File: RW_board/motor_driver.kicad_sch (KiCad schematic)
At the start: 22 parts, among them IC1 MCT8316Z0RQRGFRQ1

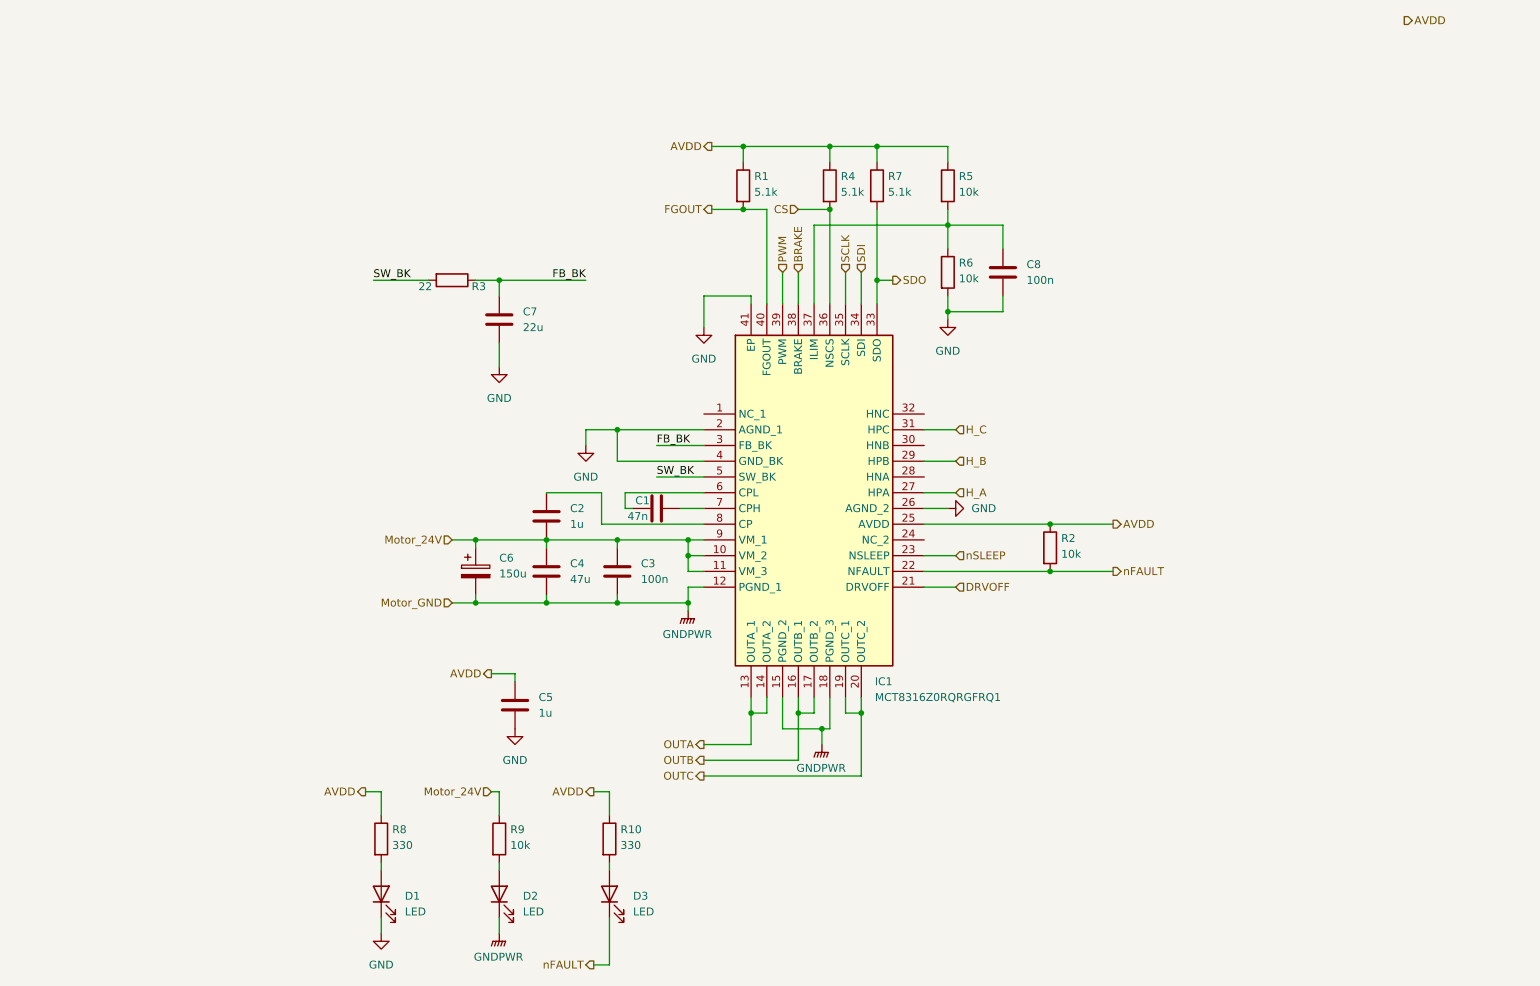
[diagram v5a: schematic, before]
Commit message: Switched motor, added connectors, finished up design
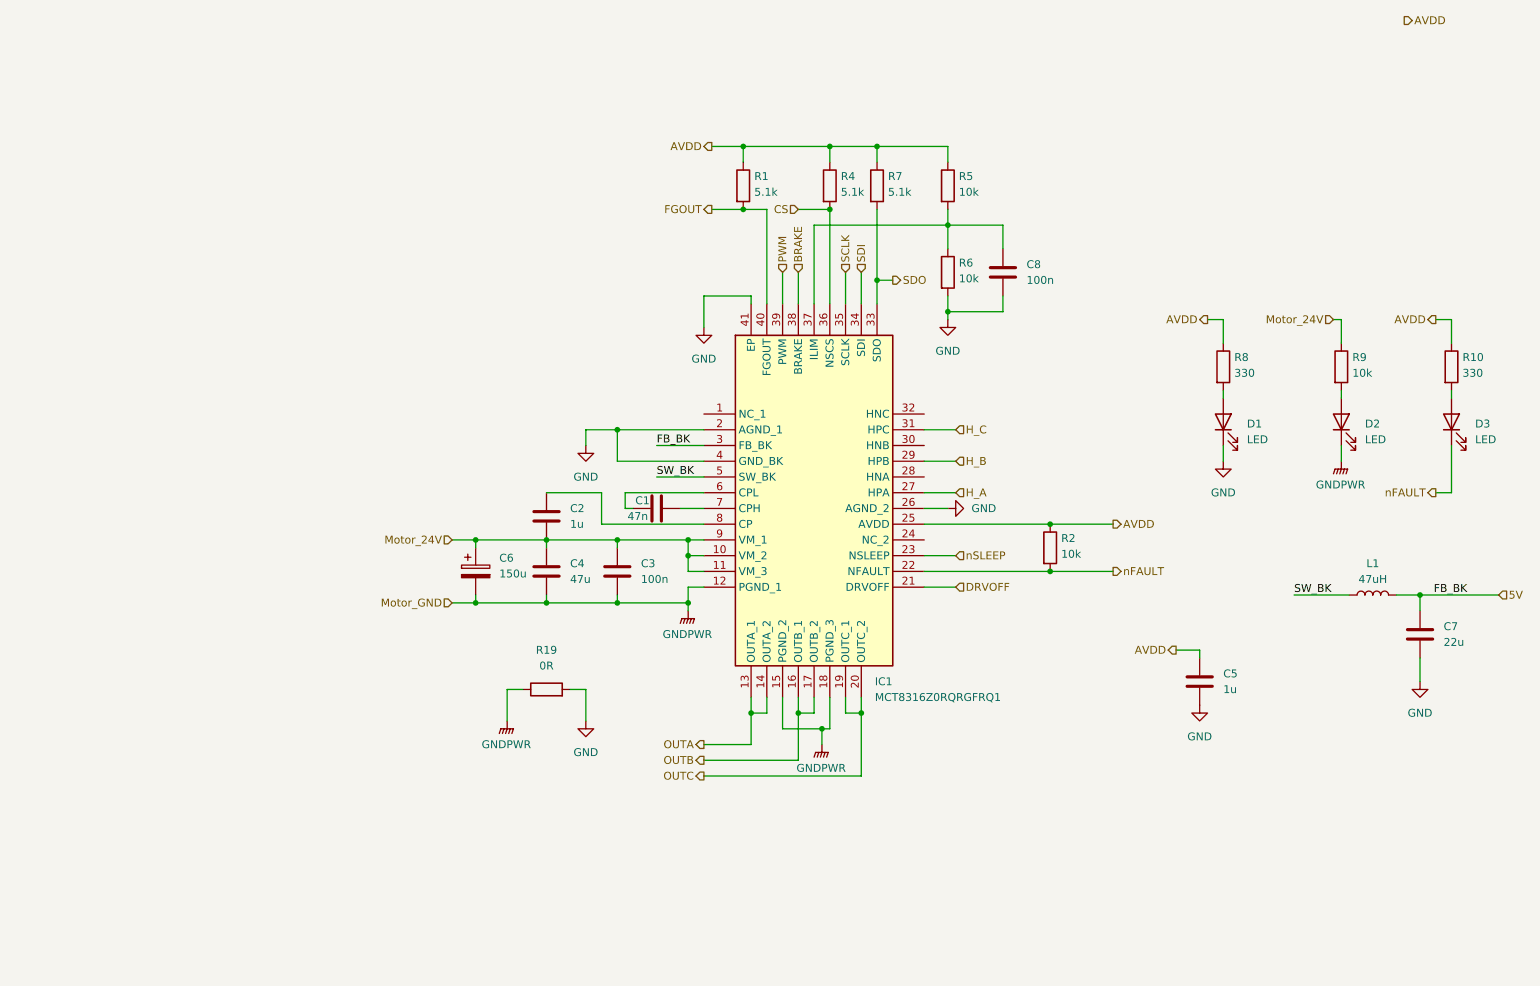
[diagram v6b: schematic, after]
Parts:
- removed R3: 22, Capacitor_SMD:C_0402_1005Metric, symbol Device:R
- added L1: 47uH, Inductor_SMD:L_1210_3225Metric, symbol Device:L
- added R19: 0R, Resistor_SMD:R_0805_2012Metric, symbol Device:R
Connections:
- net GND: now also R19.2
- net GNDPWR: now also R19.1
- net SW_BK: now also L1.1
- net FB_BK renamed 5V
- net 5V: now also L1.2
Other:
- moved on the sheet: C5, C7, D1, D2, D3, R10, R8, R9

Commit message: Fixed reset switch
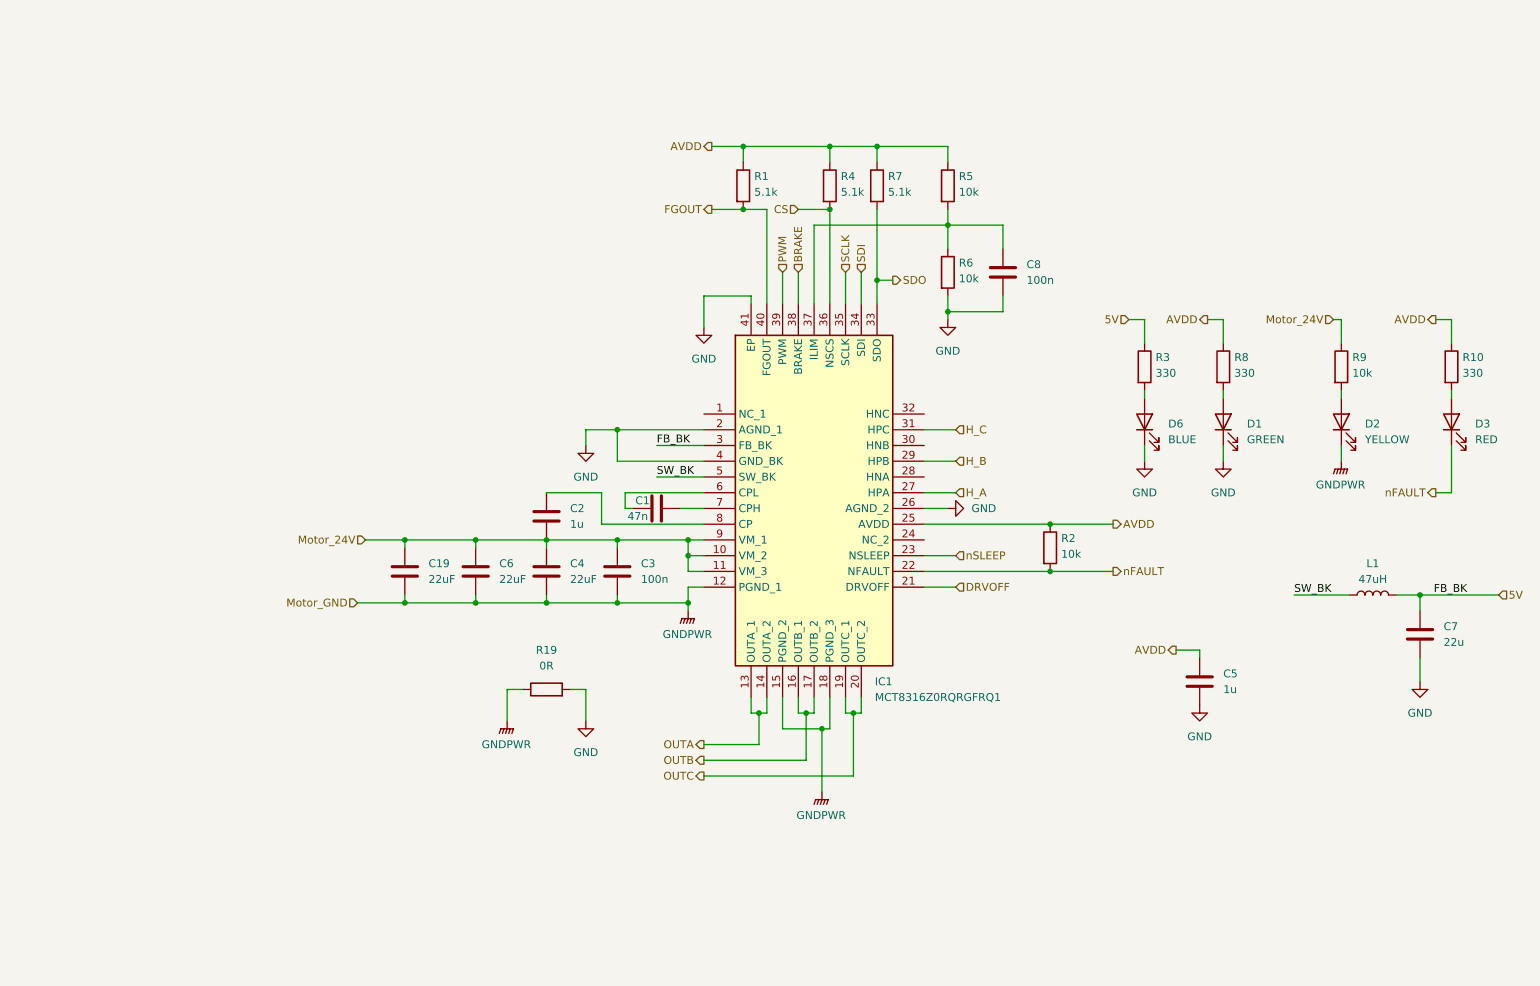
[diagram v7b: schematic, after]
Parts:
- removed C6: 150u, Capacitor_SMD:CP_Elec_6.3x7.7, symbol Device:C_Polarized
- added C19, C6: 22uF, Capacitor_SMD:C_0805_2012Metric, symbol Device:C
- added D6: BLUE, LED_SMD:LED_0603_1608Metric, symbol Device:LED
- added R3: 330, Resistor_SMD:R_0402_1005Metric, symbol Device:R
- C4: value 47u -> 22uF; Voltage rating 30V -> 35V
- D1: value LED -> GREEN; footprint (none) -> LED_SMD:LED_0603_1608Metric
- D2: value LED -> YELLOW; footprint (none) -> LED_SMD:LED_0603_1608Metric
- D3: value LED -> RED; footprint (none) -> LED_SMD:LED_0603_1608Metric
- R1, R10, R2, R4, R5, R6, R7, R8, R9: footprint (none) -> Resistor_SMD:R_0402_1005Metric
- R19: footprint Resistor_SMD:R_0805_2012Metric -> Capacitor_SMD:C_0201_0603Metric
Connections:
- net 5V: now also R3.1
- net GND: now also D6.1 (K)
- net GNDPWR: now also C19.2, C6.2
- net Motor_24V: now also C19.1, C6.1
- new net: D6.2 (A), R3.2

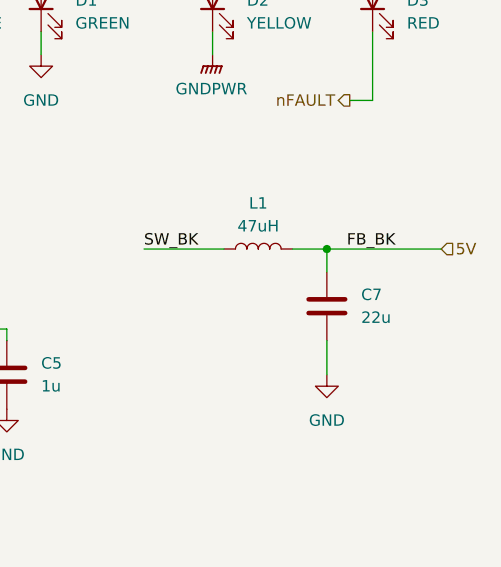
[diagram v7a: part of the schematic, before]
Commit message: Fixed text
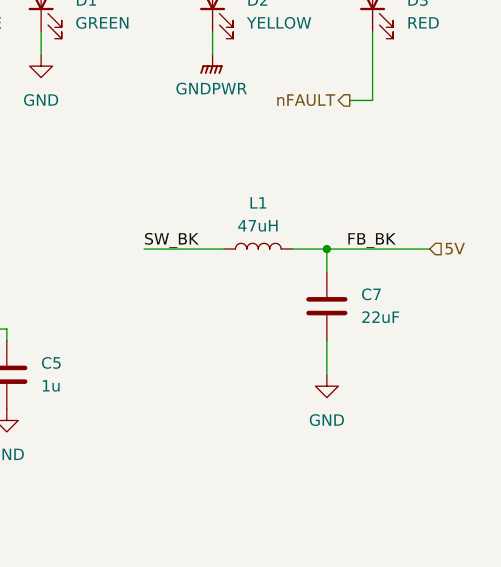
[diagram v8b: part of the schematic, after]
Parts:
- C7: value 22u -> 22uF
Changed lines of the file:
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@@
 	(wire
 		(pts
-			(xy 245.11 105.41) (xy 257.81 105.41)
+			(xy 245.11 105.41) (xy 256.54 105.41)
 		)
 		(stroke
@@
 	(hierarchical_label "5V"
 		(shape input)
-		(at 257.81 105.41 0)
+		(at 256.54 105.41 0)
 		(effects
 			(font
@@
 			)
 		)
-		(property "Value" "22u"
+		(property "Value" "22uF"
 			(at 248.92 113.0299 0)
 			(effects
